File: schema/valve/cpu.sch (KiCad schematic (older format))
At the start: 4 parts

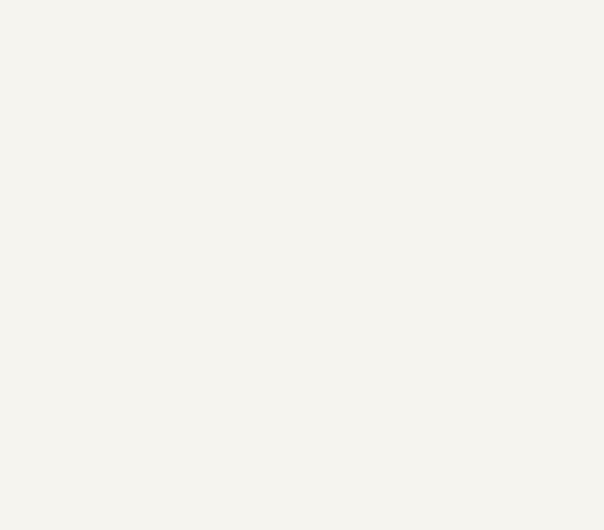
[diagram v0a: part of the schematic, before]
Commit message: Added filtering capacitors.
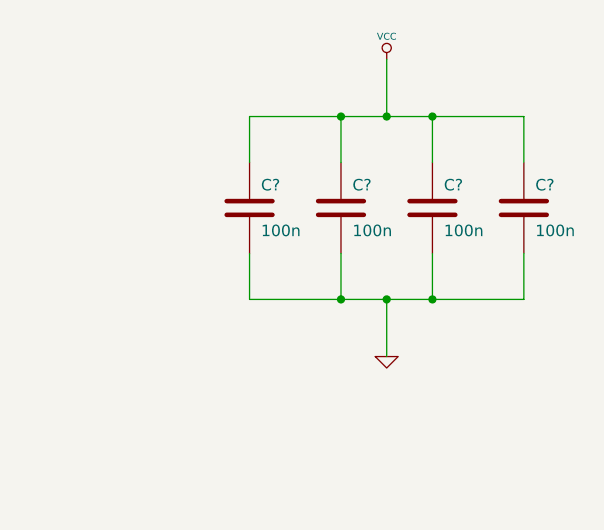
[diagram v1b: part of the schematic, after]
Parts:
- added C? (x4): 100n, symbol C
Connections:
- net GND: now also C?.2, C?.2, C?.2, C?.2
- net VCC: now also C?.1, C?.1, C?.1, C?.1
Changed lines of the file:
@@
-EESchema Schematic File Version 2  date Tue 03 Apr 2012 12:20:51 AM MSK
+EESchema Schematic File Version 2  date Tue 03 Apr 2012 01:04:14 AM MSK
 LIBS:power
 LIBS:device
@@
 $EndDescr
 $Comp
-L CRYSTAL X?
-U 1 1 4F7A0A14
-P 4900 4650
-F 0 "X?" H 4900 4800 60  0000 C CNN
-F 1 "CRYSTAL" H 4900 4500 60  0000 C CNN
-	1    4900 4650
-	0    -1   -1   0
-$EndComp
-$Comp
 L GND #PWR?
-U 1 1 4F7A09EC
-P 4350 4350
-F 0 "#PWR?" H 4350 4350 30  0001 C CNN
-F 1 "GND" H 4350 4280 30  0001 C CNN
-	1    4350 4350
+U 1 1 4F7A144A
+P 14600 2350
+F 0 "#PWR?" H 14600 2350 30  0001 C CNN
+F 1 "GND" H 14600 2280 30  0001 C CNN
+	1    14600 2350
 	1    0    0    -1
 $EndComp
+Connection ~ 14600 2100
+Wire Wire Line
+	14600 2100 14600 2350
+Connection ~ 14400 2100
+Wire Wire Line
+	14400 2100 14400 1900
+Wire Wire Line
+	15200 1900 15200 2100
+Wire Wire Line
+	15200 2100 14000 2100
+Wire Wire Line
+	14000 2100 14000 1900
+Connection ~ 14800 1300
+Wire Wire Line
+	14800 1500 14800 1300
 Wire Wire Line
 	4350 4100 4350 4350
@@
 Wire Wire Line
 	4350 2800 4350 2600
+Wire Wire Line
+	14000 1500 14000 1300
+Wire Wire Line
+	14000 1300 15200 1300
+Wire Wire Line
+	15200 1300 15200 1500
+Wire Wire Line
+	14400 1500 14400 1300
+Connection ~ 14400 1300
+Wire Wire Line
+	14800 2100 14800 1900
+Connection ~ 14800 2100
+Wire Wire Line
+	14600 1300 14600 1050
+Connection ~ 14600 1300
 $Comp
 L VCC #PWR?
+U 1 1 4F7A143F
+P 14600 1050
+F 0 "#PWR?" H 14600 1150 30  0001 C CNN
+F 1 "VCC" H 14600 1150 30  0000 C CNN
+	1    14600 1050
+	1    0    0    -1
+$EndComp
+$Comp
+L C C?
+U 1 1 4F7A141C
+P 15200 1700
+F 0 "C?" H 15250 1800 50  0000 L CNN
+F 1 "100n" H 15250 1600 50  0000 L CNN
+	1    15200 1700
+	1    0    0    -1
+$EndComp
+$Comp
+L C C?
+U 1 1 4F7A1417
+P 14800 1700
+F 0 "C?" H 14850 1800 50  0000 L CNN
+F 1 "100n" H 14850 1600 50  0000 L CNN
+	1    14800 1700
+	1    0    0    -1
+$EndComp
+$Comp
+L C C?
+U 1 1 4F7A1412
+P 14400 1700
+F 0 "C?" H 14450 1800 50  0000 L CNN
+F 1 "100n" H 14450 1600 50  0000 L CNN
+	1    14400 1700
+	1    0    0    -1
+$EndComp
+$Comp
+L C C?
+U 1 1 4F7A1406
+P 14000 1700
+F 0 "C?" H 14050 1800 50  0000 L CNN
+F 1 "100n" H 14050 1600 50  0000 L CNN
+	1    14000 1700
+	1    0    0    -1
+$EndComp
+$Comp
+L CRYSTAL X?
+U 1 1 4F7A0A14
+P 4900 4650
+F 0 "X?" H 4900 4800 60  0000 C CNN
+F 1 "CRYSTAL" H 4900 4500 60  0000 C CNN
+	1    4900 4650
+	0    -1   -1   0
+$EndComp
+$Comp
+L GND #PWR?
+U 1 1 4F7A09EC
+P 4350 4350
+F 0 "#PWR?" H 4350 4350 30  0001 C CNN
+F 1 "GND" H 4350 4280 30  0001 C CNN
+	1    4350 4350
+	1    0    0    -1
+$EndComp
+$Comp
+L VCC #PWR?

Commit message: Schema, svg and png.
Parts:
- added C3, C4: 18p, symbol C
- added C5: 1u, symbol C
- added D17, D18: LED, symbol LED
- added K1: CONN_3, symbol CONN_3
- added R112, R113: 500, symbol R
- added R114: 10k, symbol R
- added R116: 300, symbol R
- added R117, R118: 50, symbol R
- C2: renamed from C?; value C -> 100n
- R115: renamed from R?; value R -> 220k
- gave numbers to parts that had none: 6
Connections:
- net labels added: d+, d-, pwr, sin-0, sin-1, sin-10, sin-11, sin-12, sin-13, sin-14, sin-15, sin-2, sin-3, sin-4, sin-5, sin-6, sin-7, sin-8, sin-9, swclk, swdio, usb-en, vout-0, vout-1, vout-2, vout-3, vout-4, vout-5, vout-6, vout-7
- wire segments 27 -> 86
- no-connect marks 0 -> 4
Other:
- moved on the sheet: C2
